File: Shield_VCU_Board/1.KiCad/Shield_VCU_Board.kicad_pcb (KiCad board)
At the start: 2 copper layers, 250.5 x 107.1 mm, 183 parts, among them J1 Conn_02x08_Odd_Even, J10 Main_Supply, J11 Conn_01x40_Socket, J13 Conn_Molex_TouchPanel, J14 CAN_OUT, J15 Conn_01x04_Socket, J16 CAN_IN, J2 Conn_02x10_Odd_Even, J3/1 NXP3, J4 Conn_02x08_Odd_Even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

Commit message: Check on E-plan
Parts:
- moved C55 0.34 mm to (94.2, 146.1)
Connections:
- U3 pad 8: MC_SPI_SCK -> FT_T_SCK
- U3 pad 9: FT_T_SCK -> MC_SPI_SCK
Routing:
- net GND: track 804.0 -> 807.3 mm
- net Net-(U13-VIN): track 32.7 -> 29.5 mm
- net 3V3_DSPL: track 154.3 -> 153.0 mm
- net +3.7V: track 259.6 -> 260.9 mm
- net MC_SPI_SCK: track 47.3 -> 48.5 mm

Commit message: BOM v2.0 - added
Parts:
- C48, C51, C52, C53: footprint Capacitor_SMD:C_0805_2012Metric_Pad1.18x1.45mm_HandSolder -> Capacitor_SMD:C_1210_3225Metric_Pad1.33x2.70mm_HandSolder
- L3, L4: footprint Inductor_SMD:L_Pulse_PA4340 -> Inductor_SMD:L_Coilcraft_LPS4018
- NT1: value 12VTie -> GNDTie
- R2: value 634 -> 635R
- U4: value TPA6205A1 -> TPA6211A1 - ?
- moved C51 1.55 mm to (90.9, 140.2)
- moved C52 1.24 mm to (69.4, 132.2)
- moved C53 0.57 mm to (94.1, 140.2)
- moved C48 0.25 mm to (72.7, 132.2)
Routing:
- net Net-(C51-Pad1): track 25.8 -> 26.8 mm
- added copper zone on B.Cu, net Net-(C48-Pad1)
- added copper zone on B.Cu, net Net-(C51-Pad1)

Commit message: V2.21
Layout 1 ready
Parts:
- removed 3V7: 3V7, TestPoint:TestPoint_Pad_D1.0mm
- removed AUDV5, BKLTV5: TestPoint, TestPoint:TestPoint_Pad_D1.0mm
- removed C27, C29: 1uF, Capacitor_SMD:C_0805_2012Metric_Pad1.18x1.45mm_HandSolder
- removed C28, C30: 2.2uF, Capacitor_SMD:C_0805_2012Metric_Pad1.18x1.45mm_HandSolder
- removed C45, C54: 0.1uF, Capacitor_SMD:C_0805_2012Metric_Pad1.18x1.45mm_HandSolder
- removed C47: 10uF, Capacitor_SMD:C_1210_3225Metric_Pad1.33x2.70mm_HandSolder
- removed C48, C52: 22uF, Capacitor_SMD:C_1210_3225Metric_Pad1.33x2.70mm_HandSolder
- removed D13, D14: LED, LED_SMD:LED_0805_2012Metric
- removed D7, D8: MBR0540, Diode_SMD:D_SOD-123
- removed L3: 10uH, Inductor_SMD:L_Coilcraft_LPS4018
- removed NT1: GNDTie, NetTie:NetTie-2_SMD_Pad2.0mm
- removed R30, R31, R33: 0R, Resistor_SMD:R_1206_3216Metric_Pad1.30x1.75mm_HandSolder
- removed R53, R54: 1k, Resistor_SMD:R_1206_3216Metric_Pad1.30x1.75mm_HandSolder
- removed R59: 523k, Resistor_SMD:R_1206_3216Metric_Pad1.30x1.75mm_HandSolder
- removed R60: 100k, Resistor_SMD:R_1206_3216Metric_Pad1.30x1.75mm_HandSolder
- removed U12: TPS54202DDC, Package_TO_SOT_SMD:SOT-23-6
- removed U5, U6: TLV76150DCY, Package_TO_SOT_SMD:SOT-223-3_TabPin2
- added C15: 22uF, Capacitor_SMD:CP_Elec_5x5.4, B.Cu at (87.5, 140.1)
- added C21: 100uF, Capacitor_SMD:CP_Elec_5x5.4, B.Cu at (93.7, 113.2)
- R65: value 787k -> 73.2k
- R66: value 100k -> 10k
- moved FB2 37.7 mm to (105.4, 54.9), turned to 180 degrees
- moved FB1 33.7 mm to (105.4, 57.7), turned to 180 degrees
- moved 5V3 30.9 mm to (82.7, 100.4), turned to 0 degrees
- moved R34 29.8 mm to (91.5, 107.3)
- moved BAT+01 29.3 mm to (80.6, 132.8)
- moved L4 25.4 mm to (92.2, 118.6), turned to 180 degrees
- moved J10 22.9 mm to (58.1, 137.8)
- moved D15 22.9 mm to (70.4, 139.0)
- moved C55 22.9 mm to (97.6, 123.4), turned to 180 degrees
- moved C8 22.7 mm to (99.1, 57.3)
- moved R29 22.7 mm to (69.0, 94.1), turned to 180 degrees
- moved C4 21.7 mm to (79.2, 59.2), turned to 90 degrees
- moved R11 21.3 mm to (81.5, 57.1), turned to 90 degrees
- moved C49 21.2 mm to (97.5, 126.1), turned to 180 degrees
- moved R10 19.3 mm to (84.0, 57.1), turned to 90 degrees
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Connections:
- C31 pad 1: +3.7V -> +5.3V
- C33 pad 1: +3.7V -> +5.3V
- C38 pad 1: 5V_BKLT -> +5.3V
- D10 pad 1: +3.7V -> +5.3V
- D9 pad 1: +3.7V -> +5.3V
- FB2 pad 1: 5V_AUD -> +5.3V
- L2 pad 1: 5V_BKLT -> +5.3V
- R19 pad 2: 5V_BKLT -> +5.3V
- U8 pad 3: +3.7V -> +5.3V
- U9 pad 3: +3.7V -> +5.3V
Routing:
- net +3.7V: track 260.9 -> 0.00 mm, vias 2 -> 0
- net +5.3V: track 51.1 -> 287.3 mm
- net GND: track 807.3 -> 744.3 mm, vias 77 -> 68
- net BAT+: track 482.4 -> 431.1 mm, vias 0 -> 2
- net 5V_BKLT: track 33.2 -> 0.00 mm
- net Audio_L: track 13.9 -> 44.6 mm
- net Net-(C48-Pad1): track 27.0 -> 0.00 mm
- net 5V_AUD: track 25.0 -> 0.00 mm
- net Net-(U12-SW): track 21.8 -> 0.00 mm, vias 7 -> 0
- net Net-(U12-VIN): track 20.9 -> 0.00 mm
- net AUD_SHDN: track 75.0 -> 90.1 mm, vias 0 -> 2
- net Net-(U13-VIN): track 29.5 -> 36.7 mm
- net Net-(U12-FB): track 6.91 -> 0.00 mm
- net Net-(D14-A): track 6.72 -> 0.00 mm
- net Net-(U13-SW): track 23.7 -> 18.8 mm
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- removed copper zone on B.Cu, net Net-(C48-Pad1)
- removed copper zone on B.Cu, net Net-(U12-SW)

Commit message: AUDIO chip footprint correction
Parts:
- U4: footprint TPA:TPS73601DRBR -> AUD:SOP65P490X110-9L
- moved C6 2.33 mm to (78.8, 63.5)
- moved R12 0.82 mm to (87.2, 59.8)
- moved R13 0.28 mm to (87.4, 66.3)
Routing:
- net GND: track 744.3 -> 401.6 mm, vias 68 -> 52
- net GNDA: track 55.1 -> 50.4 mm, vias 2 -> 3
- net 5V0_SPKR: track 46.3 -> 44.3 mm, vias 2 -> 0
- net Net-(U4-BYPASS): track 4.23 -> 5.60 mm
- net Net-(U4-IN-): track 18.1 -> 17.4 mm
- net Net-(J8-Pin_2): track 28.6 -> 29.1 mm
- net Net-(U4-IN+): track 5.43 -> 5.97 mm

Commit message: Routing optimisations
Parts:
- moved RN8 23.6 mm to (172.0, 96.4), turned to 90 degrees
- moved C7 22.4 mm to (107.3, 84.8), turned to 180 degrees
- moved R64 21.6 mm to (173.9, 93.0), turned to 0 degrees
- moved R63 20.0 mm to (172.7, 90.7), turned to 0 degrees
- moved C16 16.6 mm to (175.9, 97.1), turned to 0 degrees
- moved C15 16.5 mm to (102.1, 132.5), turned to 0 degrees
- moved C41 15.0 mm to (175.9, 95.1), turned to 0 degrees
- moved C19 11.7 mm to (129.8, 72.7), turned to 46 degrees
- moved R62 10.3 mm to (171.8, 86.7), turned to -90 degrees
- moved R61 10.3 mm to (167.6, 96.2), turned to 180 degrees
- moved 5V3 9.19 mm to (73.5, 100.5)
- moved J8 8.55 mm to (77.9, 68.5)
- moved C12 8.27 mm to (121.6, 71.1), turned to 136 degrees
- moved C18 8.00 mm to (128.3, 71.3), turned to 46 degrees
- moved C13 7.91 mm to (122.9, 69.8), turned to 136 degrees
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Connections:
- R61 pad 1: Net-(J13-Pin_3) -> Net-(RN8-R4.2)
- R62 pad 2: Net-(J13-Pin_6) -> Net-(RN8-R1.2)
- R63 pad 1: Net-(J13-Pin_4) -> Net-(RN8-R3.2)
- R64 pad 1: Net-(J13-Pin_5) -> Net-(RN8-R2.2)
- RN8 pad 1: Net-(J13-Pin_6) -> Net-(J13-Pin_5)
- RN8 pad 2: Net-(J13-Pin_5) -> Net-(J13-Pin_6)
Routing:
- net GND: track 401.6 -> 138.6 mm, vias 52 -> 62
- net 3V3_DSPL: track 153.0 -> 188.2 mm, vias 4 -> 3
- net Net-(RN8-R1.2): track 37.8 -> 65.3 mm
- net Net-(RN8-R3.2): track 36.2 -> 63.5 mm
- net Net-(RN8-R2.2): track 37.2 -> 63.7 mm
- net Net-(J13-Pin_6): track 28.5 -> 2.35 mm
- net Net-(RN8-R4.2): track 36.0 -> 58.8 mm
- net Net-(J13-Pin_3): track 24.0 -> 2.41 mm
- net Net-(J13-Pin_4): track 26.7 -> 5.49 mm
- net Net-(J13-Pin_5): track 26.2 -> 5.08 mm
- net GNDA: track 50.4 -> 31.9 mm, vias 3 -> 12
- net AUD_SHDN: track 90.1 -> 98.3 mm
- net +1V2: track 11.3 -> 3.89 mm
- net +5.3V: track 287.3 -> 281.4 mm
- net Net-(J8-Pin_1): track 13.0 -> 8.43 mm
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
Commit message: Jumper added+ GND Sharp edges removed
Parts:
- removed R29, R32, R34: 0R, Resistor_SMD:R_1206_3216Metric_Pad1.30x1.75mm_HandSolder
- added C45: 0.1uF, Capacitor_SMD:C_0805_2012Metric_Pad1.18x1.45mm_HandSolder, B.Cu at (129.8, 65.7)
- added C46: 27pF, Capacitor_SMD:C_0805_2012Metric_Pad1.18x1.45mm_HandSolder, B.Cu at (131.8, 65.7)
- added JP1: SolderJumper_2_Open, Jumper:SolderJumper-2_P1.3mm_Open_RoundedPad1.0x1.5mm, B.Cu at (91.5, 107.4)
- added JP2: SolderJumper_2_Open, Jumper:SolderJumper-2_P1.3mm_Open_RoundedPad1.0x1.5mm, B.Cu at (80.0, 142.4)
- added JP3: SolderJumper_2_Open, Jumper:SolderJumper-2_P1.3mm_Open_TrianglePad1.0x1.5mm, B.Cu at (69.1, 94.1)
- moved R21 9.79 mm to (140.4, 72.1)
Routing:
- net GND: track 138.6 -> 143.4 mm
- net 3V3_DSPL: track 188.2 -> 190.0 mm
- net +5.3V: track 281.4 -> 283.3 mm
- net BAT+: track 428.3 -> 429.6 mm
- net Net-(JP2-B): track 36.1 -> 36.9 mm
- net Net-(JP1-A): track 25.3 -> 26.1 mm
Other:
- board text added: "Release Date: 28/06/2026"
- board text removed: "Release Date: 05/06/2026"

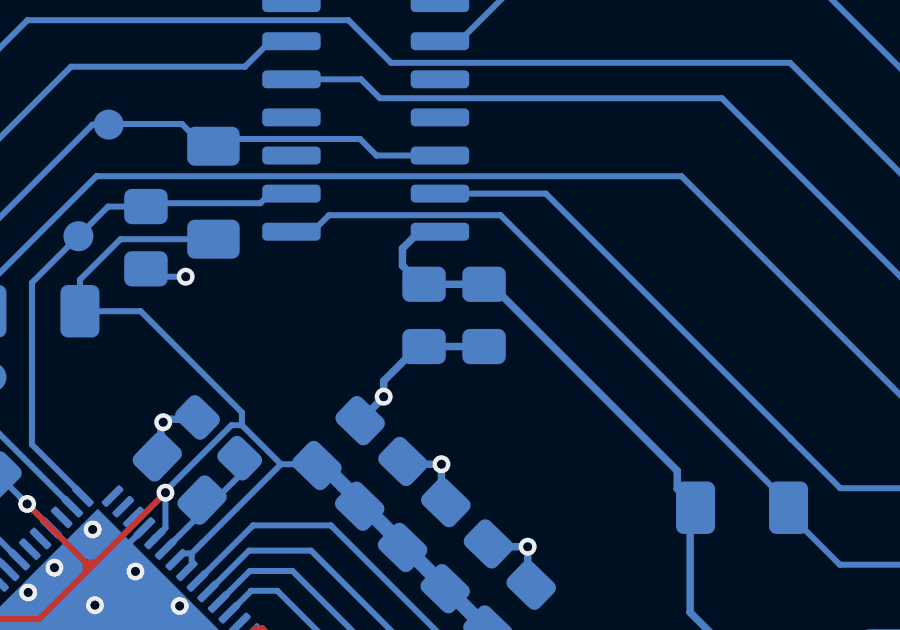
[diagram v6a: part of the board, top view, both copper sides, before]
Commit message: Swapped capacitors for schmitt inverter
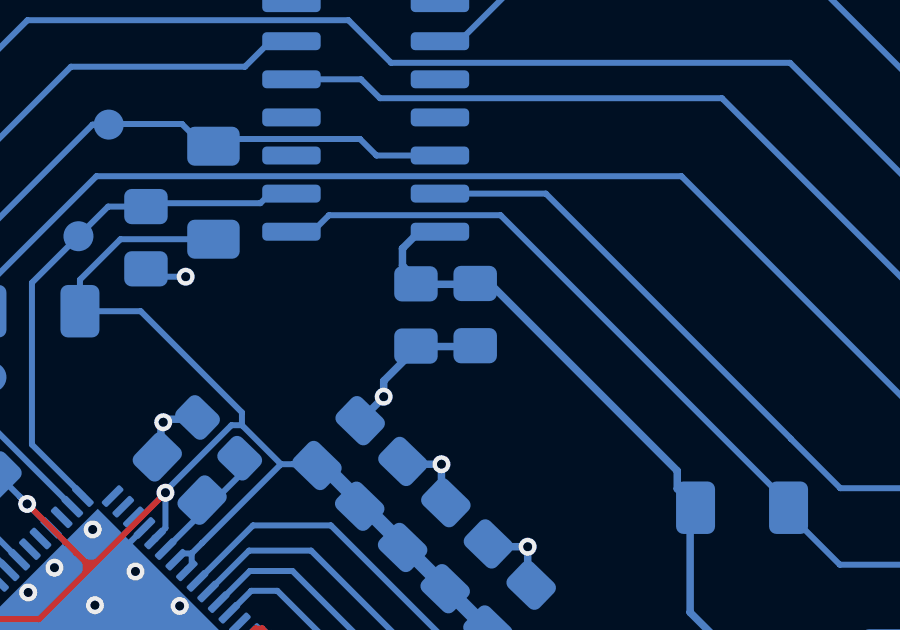
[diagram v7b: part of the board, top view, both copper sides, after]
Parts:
- moved C46 2.27 mm to (129.5, 65.7)
- moved C45 1.71 mm to (131.5, 65.6)
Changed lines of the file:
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@@
 	(footprint "Capacitor_SMD:C_0805_2012Metric_Pad1.18x1.45mm_HandSolder"
 		(layer "B.Cu")
-		(at 129.77 65.675 -90)
+		(at 131.475 65.6475 -90)
 		(descr "Capacitor SMD 0805 (2012 Metric), square (rectangular) end terminal, IPC-7351 nominal with elongated pad for handsoldering. (Body size source: IPC-SM-782 page 76, https://www.pcb-3d.com/wordpress/wp-content/uploads/ipc-sm-782a_amendment_1_and_2.pdf, https://docs.google.com/spreadsheets/d/1BsfQQcO9C6DZCsRaXUlFlo91Tg2WpOkGARC1WS5S8t0/edit?usp=sharing)")
 		(tags "capacitor handsolder")
@@
 	(footprint "Capacitor_SMD:C_0805_2012Metric_Pad1.18x1.45mm_HandSolder"
 		(layer "B.Cu")
-		(at 131.77 65.675 -90)
+		(at 129.5 65.66 -90)
 		(descr "Capacitor SMD 0805 (2012 Metric), square (rectangular) end terminal, IPC-7351 nominal with elongated pad for handsoldering. (Body size source: IPC-SM-782 page 76, https://www.pcb-3d.com/wordpress/wp-content/uploads/ipc-sm-782a_amendment_1_and_2.pdf, https://docs.google.com/spreadsheets/d/1BsfQQcO9C6DZCsRaXUlFlo91Tg2WpOkGARC1WS5S8t0/edit?usp=sharing)")
 		(tags "capacitor handsolder")
@@
 	)
 	(segment
+		(start 97.163258 130.375002)
+		(end 98.91 132.121744)
+		(width 0.5)
+		(layer "B.Cu")
+		(net "Net-(JP2-B)")
+	)
+	(segment
+		(start 98.91 132.121744)
+		(end 98.91 139.175)
+		(width 0.5)
+		(layer "B.Cu")
+		(net "Net-(JP2-B)")
+	)
+	(segment
+		(start 97.163258 129.944999)
+		(end 97.163258 130.375002)
+		(width 0.5)
+		(layer "B.Cu")
+		(net "Net-(JP2-B)")
+	)
+	(segment
+		(start 98.488256 126.35)
+		(end 97.150755 127.6875)
+		(width 0.5)
+		(layer "B.Cu")
+		(net "Net-(JP2-B)")
+	)
+	(segment
+		(start 98.488256 124.129244)
+		(end 99.1925 123.425)
+		(width 0.5)
+		(layer "B.Cu")
+		(net "Net-(JP2-B)")
+	)
+	(segment
+		(start 97.150755 127.6875)
+		(end 97.150756 129.932498)
+		(width 0.5)
+		(layer "B.Cu")
+		(net "Net-(JP2-B)")
+	)
+	(segment
+		(start 98.488256 126.085)
+		(end 98.488256 124.129244)
+		(width 0.5)
+		(layer "B.Cu")
+		(net "Net-(JP2-B)")
+	)
+	(segment
+		(start 98.488256 126.084999)
+		(end 98.488256 126.35)
+		(width 0.5)
+		(layer "B.Cu")
+		(net "Net-(JP2-B)")
+	)
+	(segment
+		(start 95.69 142.395)
+		(end 80.629999 142.395)
+		(width 0.5)
+		(layer "B.Cu")
+		(net "Net-(JP2-B)")
+	)
+	(segment
+		(start 98.91 139.175)
+		(end 95.69 142.395)
+		(width 0.5)
+		(layer "B.Cu")
+		(net "Net-(JP2-B)")
+	)
+	(segment
+		(start 97.150756 129.932498)
+		(end 97.163257 129.944999)
+		(width 0.5)
+		(layer "B.Cu")
+		(net "Net-(JP2-B)")
+	)
+	(segment
 		(start 97.150756 132.2325)
 		(end 97.150752 135.935001)
@@
 	)
 	(segment
+		(start 90.395 120.08)
+		(end 90.395 118.559999)
+		(width 0.5)
+		(layer "B.Cu")
+		(net "Net-(JP1-A)")
+	)
+	(segment
+		(start 89.852669 133.55767)
+		(end 89.852669 126.015067)
+		(width 0.5)
+		(layer "B.Cu")
+		(net "Net-(JP1-A)")
+	)
+	(segment
+		(start 90.4 120.176628)
+		(end 90.4 120.085)
+		(width 0.5)
+		(layer "B.Cu")
+		(net "Net-(JP1-A)")
+	)
+	(segment
+		(start 89.852669 120.723959)
+		(end 90.4 120.176628)
+		(width 0.5)
+		(layer "B.Cu")
+		(net "Net-(JP1-A)")
+	)
+	(segment
+		(start 91.49 113.225)
+		(end 91.49 108.084999)
+		(width 0.5)
+		(layer "B.Cu")
+		(net "Net-(JP1-A)")
+	)
+	(segment
+		(start 90.4 120.085)
+		(end 90.395 120.08)
+		(width 0.5)
+		(layer "B.Cu")
+		(net "Net-(JP1-A)")
+	)
+	(segment
+		(start 89.852669 126.015067)
+		(end 89.852669 120.723959)
+		(width 0.5)
+		(layer "B.Cu")
+		(net "Net-(JP1-A)")
+	)
+	(segment
+		(start 93.899999 137.605)
+		(end 89.852669 133.55767)
+		(width 0.5)
+		(layer "B.Cu")
+		(net "Net-(JP1-A)")
+	)
+	(segment
+		(start 91.49 108.084999)
+		(end 91.47 108.064999)
+		(width 0.5)
+		(layer "B.Cu")
+		(net "Net-(JP1-A)")
+	)
+	(segment
 		(start 263.474999 95.734999)
 		(end 261.462499 93.7225)
@@
 		(net "unconnected-(J2-Pin_20-Pad20)")
 	)
-	(segment
-		(start 97.163258 130.375002)
-		(end 98.91 132.121744)
-		(width 0.5)
-		(layer "B.Cu")
-		(net "Net-(JP2-B)")
-	)
-	(segment
-		(start 98.91 132.121744)
-		(end 98.91 139.175)
-		(width 0.5)
-		(layer "B.Cu")
-		(net "Net-(JP2-B)")
-	)
-	(segment
-		(start 97.163258 129.944999)
-		(end 97.163258 130.375002)
-		(width 0.5)
-		(layer "B.Cu")
-		(net "Net-(JP2-B)")
-	)
-	(segment
-		(start 98.488256 126.35)
-		(end 97.150755 127.6875)
-		(width 0.5)
-		(layer "B.Cu")
-		(net "Net-(JP2-B)")
-	)
-	(segment
-		(start 98.488256 124.129244)
-		(end 99.1925 123.425)
-		(width 0.5)
-		(layer "B.Cu")
-		(net "Net-(JP2-B)")
-	)
-	(segment
-		(start 97.150755 127.6875)
-		(end 97.150756 129.932498)
-		(width 0.5)
-		(layer "B.Cu")
-		(net "Net-(JP2-B)")
-	)
-	(segment
-		(start 98.488256 126.085)
-		(end 98.488256 124.129244)
-		(width 0.5)
-		(layer "B.Cu")
-		(net "Net-(JP2-B)")
-	)
-	(segment
-		(start 98.488256 126.084999)
-		(end 98.488256 126.35)
-		(width 0.5)
-		(layer "B.Cu")
-		(net "Net-(JP2-B)")
-	)
-	(segment
-		(start 95.69 142.395)
-		(end 80.629999 142.395)
-		(width 0.5)
-		(layer "B.Cu")
-		(net "Net-(JP2-B)")
-	)
-	(segment
-		(start 98.91 139.175)
-		(end 95.69 142.395)
-		(width 0.5)
-		(layer "B.Cu")
-		(net "Net-(JP2-B)")
-	)
-	(segment
-		(start 97.150756 129.932498)
-		(end 97.163257 129.944999)
-		(width 0.5)
-		(layer "B.Cu")
-		(net "Net-(JP2-B)")
-	)
-	(segment
-		(start 90.395 120.08)
-		(end 90.395 118.559999)
-		(width 0.5)
-		(layer "B.Cu")
-		(net "Net-(JP1-A)")
-	)
-	(segment
-		(start 89.852669 133.55767)
-		(end 89.852669 126.015067)
-		(width 0.5)
-		(layer "B.Cu")
-		(net "Net-(JP1-A)")
-	)
-	(segment
-		(start 90.4 120.176628)
-		(end 90.4 120.085)
-		(width 0.5)
-		(layer "B.Cu")
-		(net "Net-(JP1-A)")
-	)
-	(segment
-		(start 89.852669 120.723959)
-		(end 90.4 120.176628)
-		(width 0.5)
-		(layer "B.Cu")
-		(net "Net-(JP1-A)")
-	)
-	(segment
-		(start 91.49 113.225)
-		(end 91.49 108.084999)
-		(width 0.5)
-		(layer "B.Cu")
-		(net "Net-(JP1-A)")
-	)
-	(segment
-		(start 90.4 120.085)
-		(end 90.395 120.08)
-		(width 0.5)
-		(layer "B.Cu")
-		(net "Net-(JP1-A)")
-	)
-	(segment
-		(start 89.852669 126.015067)
-		(end 89.852669 120.723959)
-		(width 0.5)
-		(layer "B.Cu")
-		(net "Net-(JP1-A)")
-	)
-	(segment
-		(start 93.899999 137.605)
-		(end 89.852669 133.55767)
-		(width 0.5)
-		(layer "B.Cu")
-		(net "Net-(JP1-A)")
-	)
-	(segment
-		(start 91.49 108.084999)
-		(end 91.47 108.064999)
-		(width 0.5)
-		(layer "B.Cu")
-		(net "Net-(JP1-A)")
-	)
 	(zone
